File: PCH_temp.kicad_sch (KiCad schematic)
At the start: 1 part

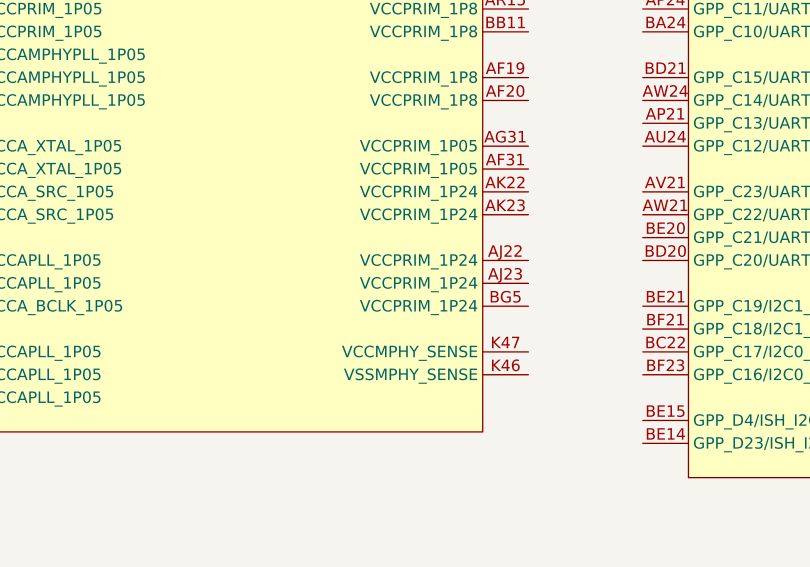
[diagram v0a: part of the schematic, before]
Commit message: Fixed some PCH pin names
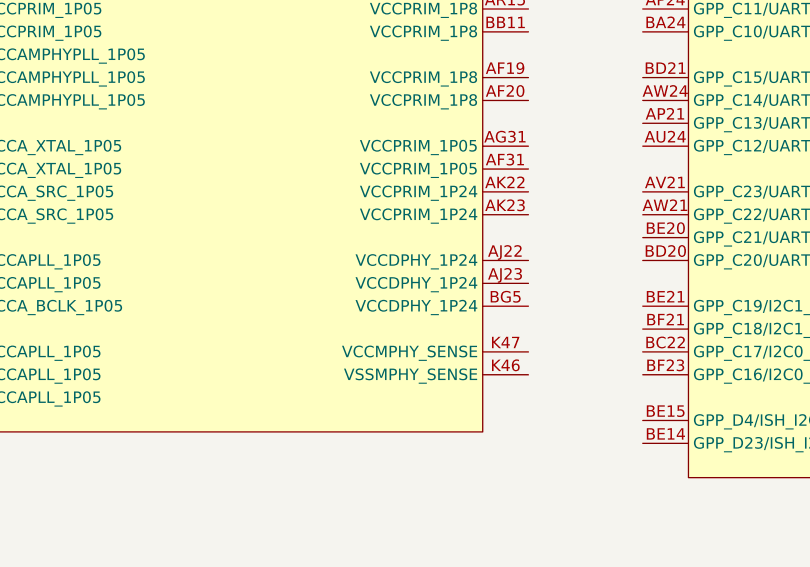
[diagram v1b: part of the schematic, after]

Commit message: replaced PCH symbol set with modified more sane version
seriously what was intel thinking when laying out half of those symbols, i can't make sense of their choices
if you want the original version take it from the commit before this one I guess
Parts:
- removed UPCH1: Intel Cannon Point 300-Series Platform Controller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, A-my-stuff:CNP-H_BGA_874P-T, symbol A-my-stuff:Intel_CFL_PCH_FCBGA874
- added UPCH1: Intel Cannon Point 300-Series Platform Controller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, A-my-stuff:CNP-H_BGA_874P-T, symbol A-my-stuff:Intel_CFL_PCH_FCBGA874_but_better

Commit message: Connected DMI for fun (with lane reversal)
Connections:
- net GND: now reaches UPCH1.BG3 (VSS)
- net GND: now also UPCH1.A2 (VSS), UPCH1.A28 (VSS), UPCH1.A3 (VSS), UPCH1.A33 (VSS), UPCH1.A37 (VSS), UPCH1.A4 (VSS), UPCH1.A45 (VSS), UPCH1.A46 (VSS), UPCH1.A47 (VSS), UPCH1.A48 (VSS), UPCH1.A5 (VSS), UPCH1.A8 (VSS), UPCH1.AA19 (VSS), UPCH1.AA20 (VSS), UPCH1.AA25 (VSS), UPCH1.AA27 (VSS), UPCH1.AA28 (VSS), UPCH1.AA30 (VSS), UPCH1.AA31 (VSS), UPCH1.AA49 (VSS), UPCH1.AA5 (VSS), UPCH1.AB19 (VSS), UPCH1.AB25 (VSS), UPCH1.AB31 (VSS), UPCH1.AC12 (VSS), UPCH1.AC17 (VSS), UPCH1.AC33 (VSS), UPCH1.AC38 (VSS), UPCH1.AC4 (VSS), UPCH1.AC46 (VSS), UPCH1.AD1 (VSS), UPCH1.AD19 (VSS), UPCH1.AD2 (VSS), UPCH1.AD22 (VSS), UPCH1.AD25 (VSS), UPCH1.AD49 (VSS), UPCH1.AE12 (VSS), UPCH1.AE33 (VSS), UPCH1.AE38 (VSS), UPCH1.AE4 (VSS), UPCH1.AE46 (VSS), UPCH1.AF22 (VSS), UPCH1.AF25 (VSS), UPCH1.AF28 (VSS), UPCH1.AG1 (VSS), UPCH1.AG22 (VSS), UPCH1.AG23 (VSS), UPCH1.AG25 (VSS), UPCH1.AG27 (VSS), UPCH1.AG28 (VSS), UPCH1.AG30 (VSS), UPCH1.AG49 (VSS), UPCH1.AH12 (VSS), UPCH1.AH17 (VSS), UPCH1.AH33 (VSS), UPCH1.AH38 (VSS), UPCH1.AJ19 (VSS), UPCH1.AJ20 (VSS), UPCH1.AJ25 (VSS), UPCH1.AJ27 (VSS), UPCH1.AJ28 (VSS), UPCH1.AJ30 (VSS), UPCH1.AJ31 (VSS), UPCH1.AK19 (VSS), UPCH1.AK20 (VSS), UPCH1.AK25 (VSS), UPCH1.AK27 (VSS), UPCH1.AK28 (VSS), UPCH1.AK30 (VSS), UPCH1.AK31 (VSS), UPCH1.AK4 (VSS), UPCH1.AK46 (VSS), UPCH1.AL12 (VSS), UPCH1.AL17 (VSS), UPCH1.AL21 (VSS), UPCH1.AL24 (VSS), UPCH1.AL26 (VSS), UPCH1.AL29 (VSS), UPCH1.AL33 (VSS), UPCH1.AL38 (VSS), UPCH1.AM1 (VSS), UPCH1.AM18 (VSS), UPCH1.AM32 (VSS), UPCH1.AM49 (VSS), UPCH1.AN12 (VSS), UPCH1.AN16 (VSS), UPCH1.AN34 (VSS), UPCH1.AN38 (VSS), UPCH1.AP4 (VSS), UPCH1.AP46 (VSS), UPCH1.AR12 (VSS), UPCH1.AR16 (VSS), UPCH1.AR34 (VSS), UPCH1.AR38 (VSS), UPCH1.AT1 (VSS), UPCH1.AT16 (VSS), UPCH1.AT18 (VSS), UPCH1.AT21 (VSS), UPCH1.AT24 (VSS), UPCH1.AT26 (VSS), UPCH1.AT29 (VSS), UPCH1.AT32 (VSS), UPCH1.AT34 (VSS), UPCH1.AT45 (VSS), UPCH1.AV11 (VSS), UPCH1.AV39 (VSS), UPCH1.AW10 (VSS), UPCH1.AW4 (VSS), UPCH1.AW40 (VSS), UPCH1.AW46 (VSS), UPCH1.B47 (VSS), UPCH1.B48 (VSS), UPCH1.B49 (VSS), UPCH1.BA12 (VSS), UPCH1.BA14 (VSS), UPCH1.BA44 (VSS), UPCH1.BA5 (VSS), UPCH1.BA6 (VSS), UPCH1.BB41 (VSS), UPCH1.BB43 (VSS), UPCH1.BB9 (VSS), UPCH1.BC10 (VSS), UPCH1.BC13 (VSS), UPCH1.BC15 (VSS), UPCH1.BC19 (VSS), UPCH1.BC24 (VSS), UPCH1.BC26 (VSS), UPCH1.BC31 (VSS), UPCH1.BC35 (VSS), UPCH1.BC40 (VSS), UPCH1.BC45 (VSS), UPCH1.BC8 (VSS), UPCH1.BD43 (VSS), UPCH1.BE44 (VSS), UPCH1.BF1 (VSS), UPCH1.BF2 (VSS), UPCH1.BF3 (VSS), UPCH1.BF48 (VSS), UPCH1.BF49 (VSS), UPCH1.BG17 (VSS), UPCH1.BG2 (VSS), UPCH1.BG22 (VSS), UPCH1.BG25 (VSS), UPCH1.BG28 (VSS), UPCH1.BG33 (VSS), UPCH1.BG37 (VSS), UPCH1.BG4 (VSS), UPCH1.BG48 (VSS), UPCH1.C12 (VSS), UPCH1.C25 (VSS), UPCH1.C30 (VSS), UPCH1.C4 (VSS), UPCH1.C48 (VSS), UPCH1.C5 (VSS), UPCH1.D12 (VSS), UPCH1.D16 (VSS), UPCH1.D17 (VSS), UPCH1.D30 (VSS), UPCH1.D33 (VSS), UPCH1.D8 (VSS), UPCH1.E10 (VSS), UPCH1.E13 (VSS), UPCH1.E15 (VSS), UPCH1.E17 (VSS), UPCH1.E19 (VSS), UPCH1.E22 (VSS), UPCH1.E24 (VSS), UPCH1.E26 (VSS), UPCH1.E31 (VSS), UPCH1.E33 (VSS), UPCH1.E35 (VSS), UPCH1.E40 (VSS), UPCH1.E42 (VSS), UPCH1.E8 (VSS), UPCH1.F41 (VSS), UPCH1.F43 (VSS), UPCH1.F47 (VSS), UPCH1.G44 (VSS), UPCH1.G6 (VSS), UPCH1.H8 (VSS), UPCH1.J10 (VSS), UPCH1.J26 (VSS), UPCH1.J29 (VSS), UPCH1.J4 (VSS), UPCH1.J40 (VSS), UPCH1.J46 (VSS), UPCH1.J47 (VSS), UPCH1.J48 (VSS), UPCH1.J9 (VSS), UPCH1.K11 (VSS), UPCH1.K39 (VSS), UPCH1.M16 (VSS), UPCH1.M18 (VSS), UPCH1.M21 (VSS), UPCH1.M24 (VSS), UPCH1.M32 (VSS), UPCH1.M34 (VSS), UPCH1.M49 (VSS), UPCH1.M5 (VSS), UPCH1.N12 (VSS), UPCH1.N16 (VSS), UPCH1.N34 (VSS), UPCH1.N35 (VSS), UPCH1.N37 (VSS), UPCH1.N38 (VSS), UPCH1.P26 (VSS), UPCH1.P29 (VSS), UPCH1.P4 (VSS), UPCH1.P46 (VSS), UPCH1.R12 (VSS), UPCH1.R16 (VSS), UPCH1.R26 (VSS), UPCH1.R29 (VSS), UPCH1.R3 (VSS), UPCH1.R34 (VSS), UPCH1.R38 (VSS), UPCH1.R4 (VSS), UPCH1.T17 (VSS), UPCH1.T18 (VSS), UPCH1.T32 (VSS), UPCH1.T4 (VSS), UPCH1.T49 (VSS), UPCH1.T5 (VSS), UPCH1.T7 (VSS), UPCH1.U12 (VSS), UPCH1.U15 (VSS), UPCH1.U17 (VSS), UPCH1.U21 (VSS), UPCH1.U24 (VSS), UPCH1.U33 (VSS), UPCH1.U38 (VSS), UPCH1.V20 (VSS), UPCH1.V22 (VSS), UPCH1.V4 (VSS), UPCH1.V46 (VSS), UPCH1.W25 (VSS), UPCH1.W27 (VSS), UPCH1.W28 (VSS), UPCH1.W30 (VSS), UPCH1.Y10 (VSS), UPCH1.Y12 (VSS), UPCH1.Y17 (VSS), UPCH1.Y33 (VSS), UPCH1.Y38 (VSS), UPCH1.Y9 (VSS)
- net DMI_CRx_PTx_0+: now reaches UPCH1.B29 (DMI3_TXP)
- net DMI_CRx_PTx_1+: now reaches UPCH1.B31 (DMI2_TXP)
- net DMI_CRx_PTx_2+: now reaches UPCH1.B32 (DMI1_TXP)
- net DMI_CRx_PTx_3+: now reaches UPCH1.B33 (DMI0_TXP)
- net DMI_CRx_PTx_0-: now reaches UPCH1.C29 (DMI3_TXN)
- net DMI_CRx_PTx_1-: now reaches UPCH1.C31 (DMI2_TXN)
- net DMI_CRx_PTx_2-: now reaches UPCH1.C32 (DMI1_TXN)
- net DMI_CRx_PTx_3-: now reaches UPCH1.C33 (DMI0_TXN)
- net DMI_CTx_PRx_0+: now reaches UPCH1.F30 (DMI3_RXP)
- net DMI_CTx_PRx_2+: now reaches UPCH1.F34 (DMI1_RXP)
- net DMI_CTx_PRx_0-: now reaches UPCH1.G30 (DMI3_RXN)
- net DMI_CTx_PRx_2-: now reaches UPCH1.G33 (DMI1_RXN)
- net DMI_CTx_PRx_1+: now reaches UPCH1.J32 (DMI2_RXP)
- net DMI_CTx_PRx_3+: now reaches UPCH1.J35 (DMI0_RXP)
- net DMI_CTx_PRx_1-: now reaches UPCH1.K32 (DMI2_RXN)
- net DMI_CTx_PRx_3-: now reaches UPCH1.K34 (DMI0_RXN)
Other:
- moved on the sheet: UPCH1I, UPCH1J, UPCH1L
